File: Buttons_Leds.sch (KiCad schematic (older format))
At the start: 38 parts, among them P11 SwPins, P12 PinLeds, Q2 BC849, Q3 BC849, Q4 BC849, Q5 BC849, SW1 TEC_1, SW2 TEC_1, SW3 TEC_1, SW4 TEC_1

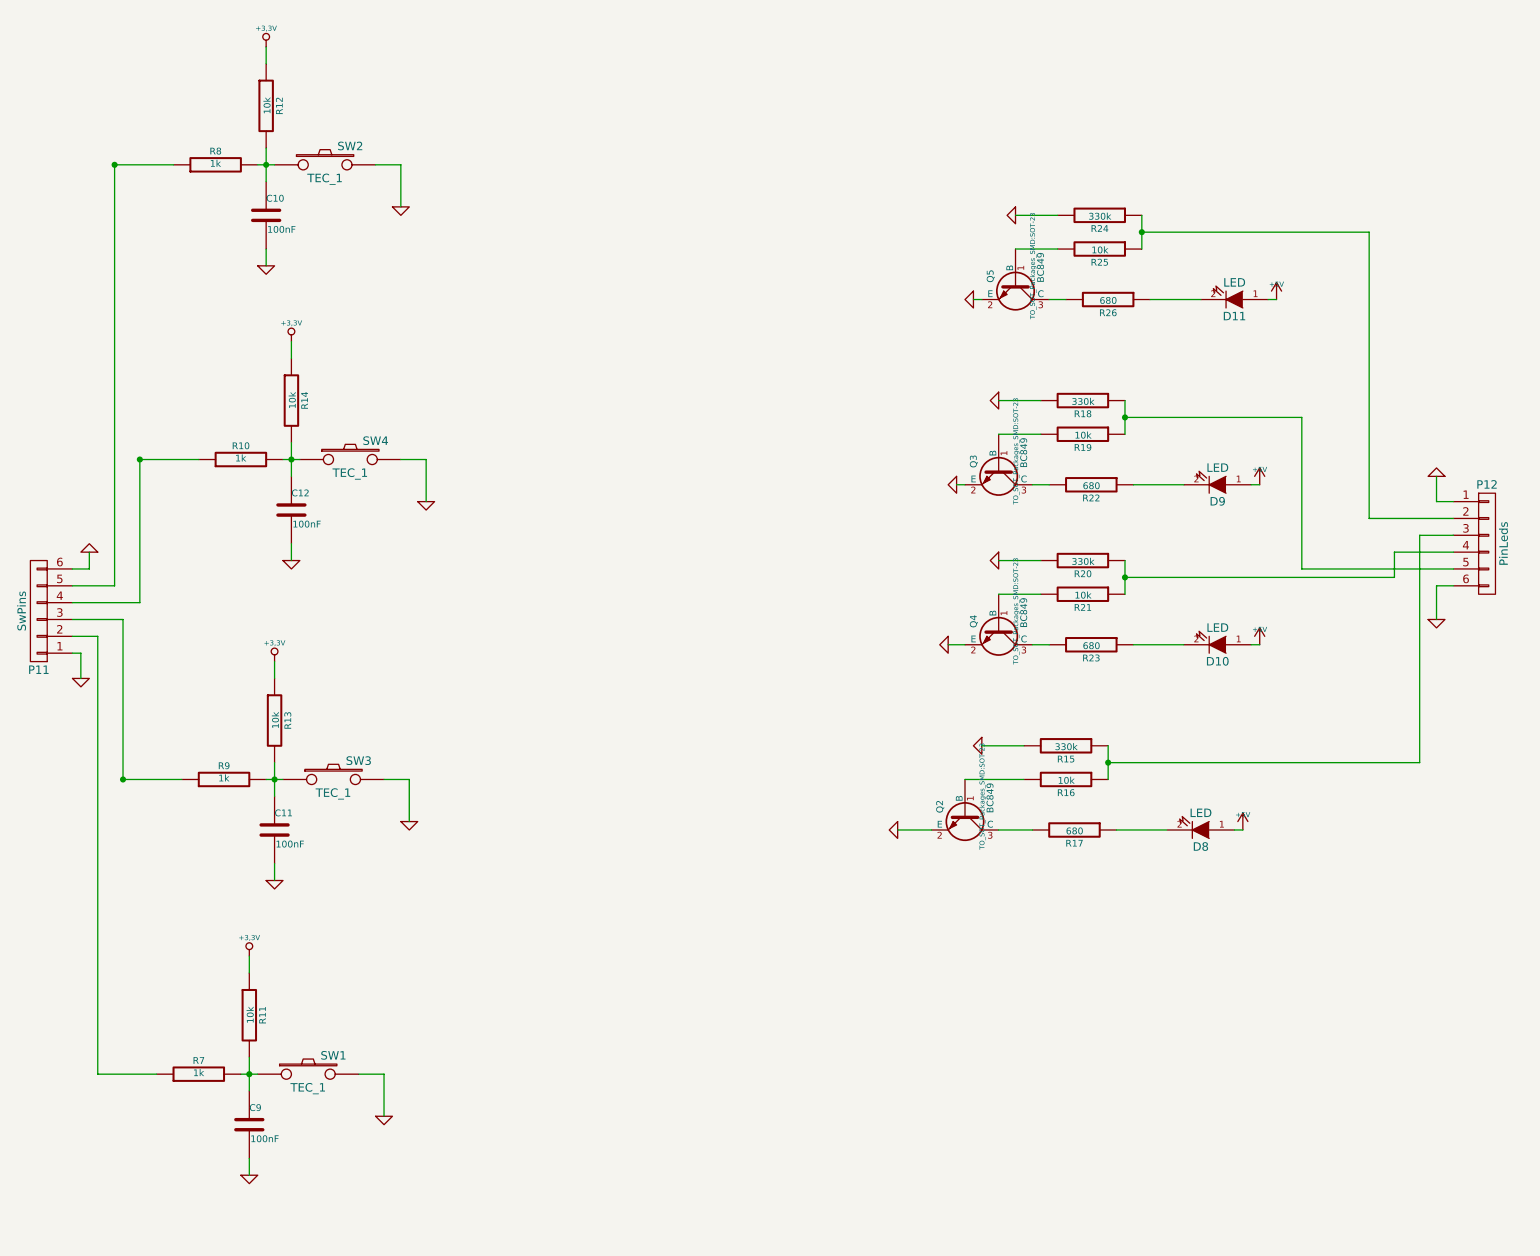
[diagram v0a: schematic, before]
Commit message: Add digikey code and comment schematic.
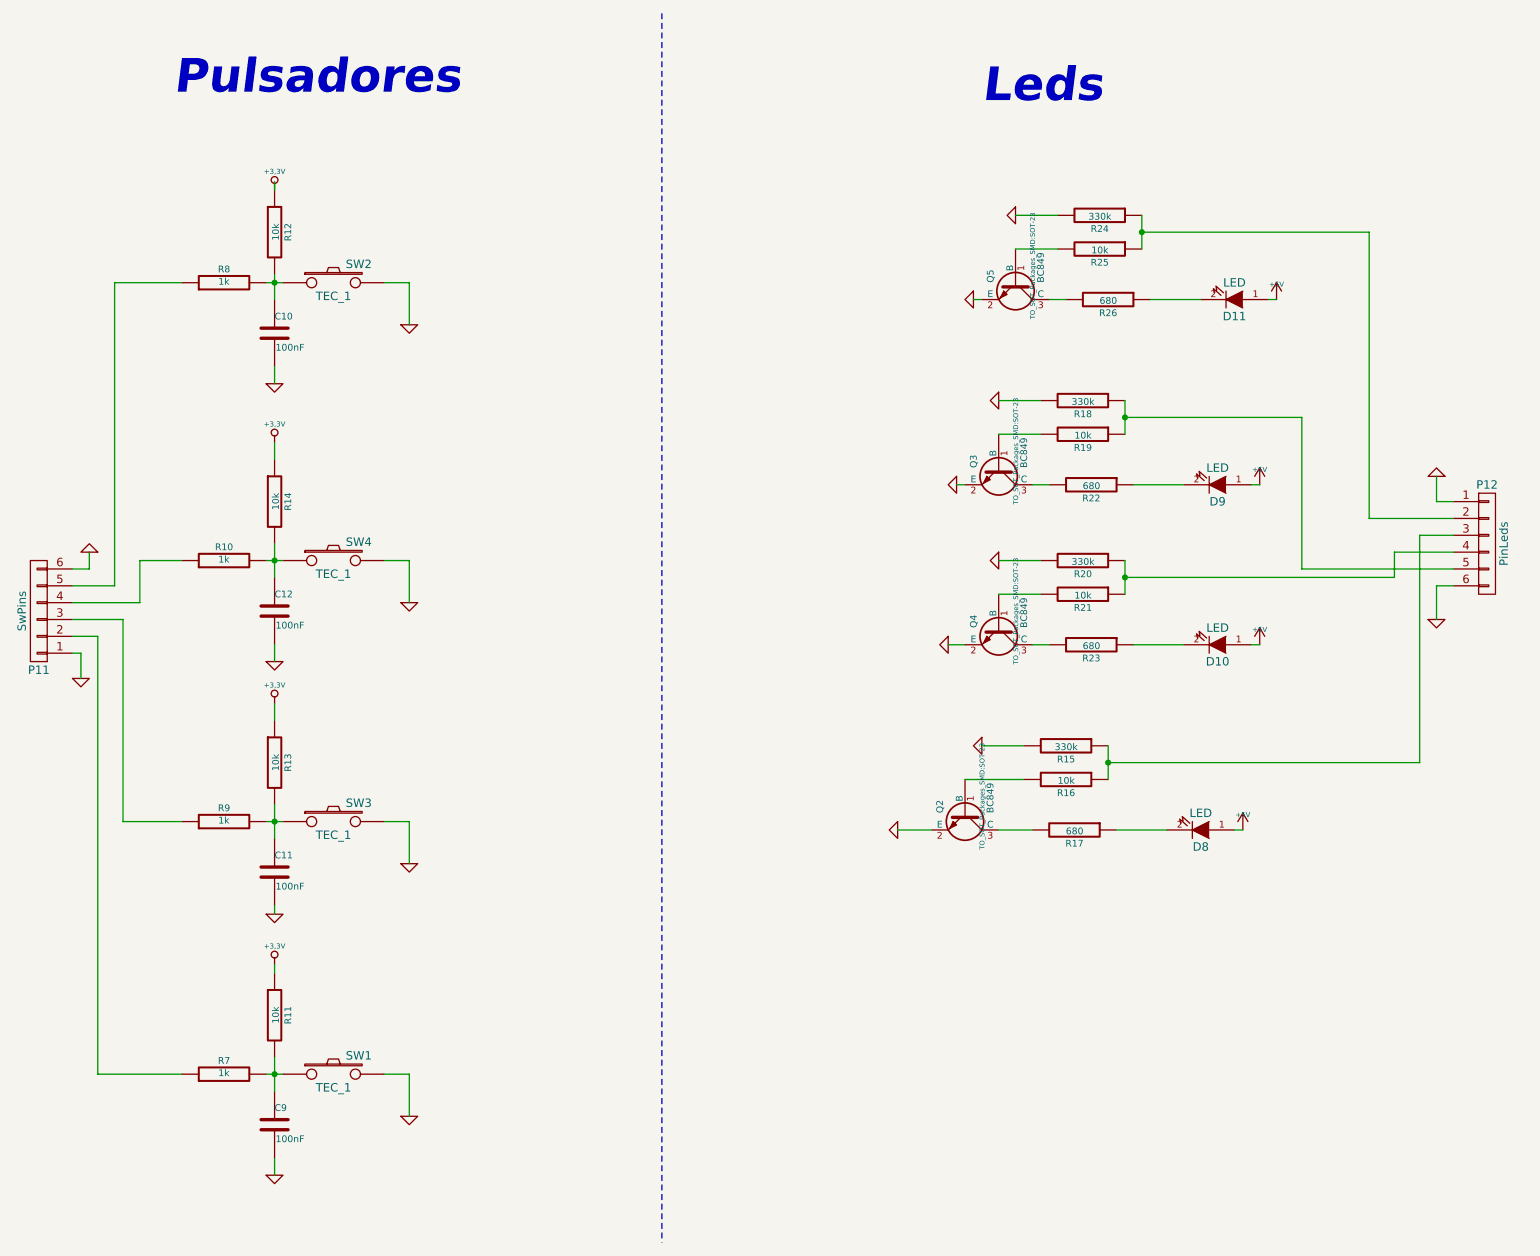
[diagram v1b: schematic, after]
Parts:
- C10, C11, C12, C9: Digikey 399-1167-1-ND -> (none); Digikey# (none) -> 399-1167-1-ND
- D10, D11, D8, D9: Digikey 1080-1410-1-ND -> (none); Digikey# (none) -> 1080-1410-1-ND
- P11, P12: Digikey# (none) -> 1528-1074-ND
- Q2, Q3, Q4, Q5: Digikey# (none) -> BC849BLT1GOSTR-ND
- R10, R7, R8, R9: Digikey 311-1.0KARCT-ND -> (none); Digikey# (none) -> 311-1.0KARCT-ND
- R11, R12, R13, R14, R16, R19, R21, R25: Digikey P10KACT-ND -> (none); Digikey# (none) -> P10KACT-ND
- R15, R18, R20, R24: Digikey RMCF0805JT330KCT-ND -> (none); Digikey# (none) -> RMCF0805JT330KCT-ND
- R17, R22, R23, R26: Digikey RR12P680DCT-ND -> (none); Digikey# (none) -> RR12P680DCT-ND
- SW1, SW2, SW3, SW4: Digikey 450-1804-ND -> (none); Digikey# (none) -> 450-1804-ND
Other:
- note added: "Leds"
- note added: "Pulsadores"
- moved on the sheet: C10, C11, C12, C9, R10, R11, R12, R13, R14, R7, R8, R9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

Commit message: Actualizo las revisiones y documentaciones faltante. Algunas correcciones realizadas, faltan algunas mas que vere de hacerlas.
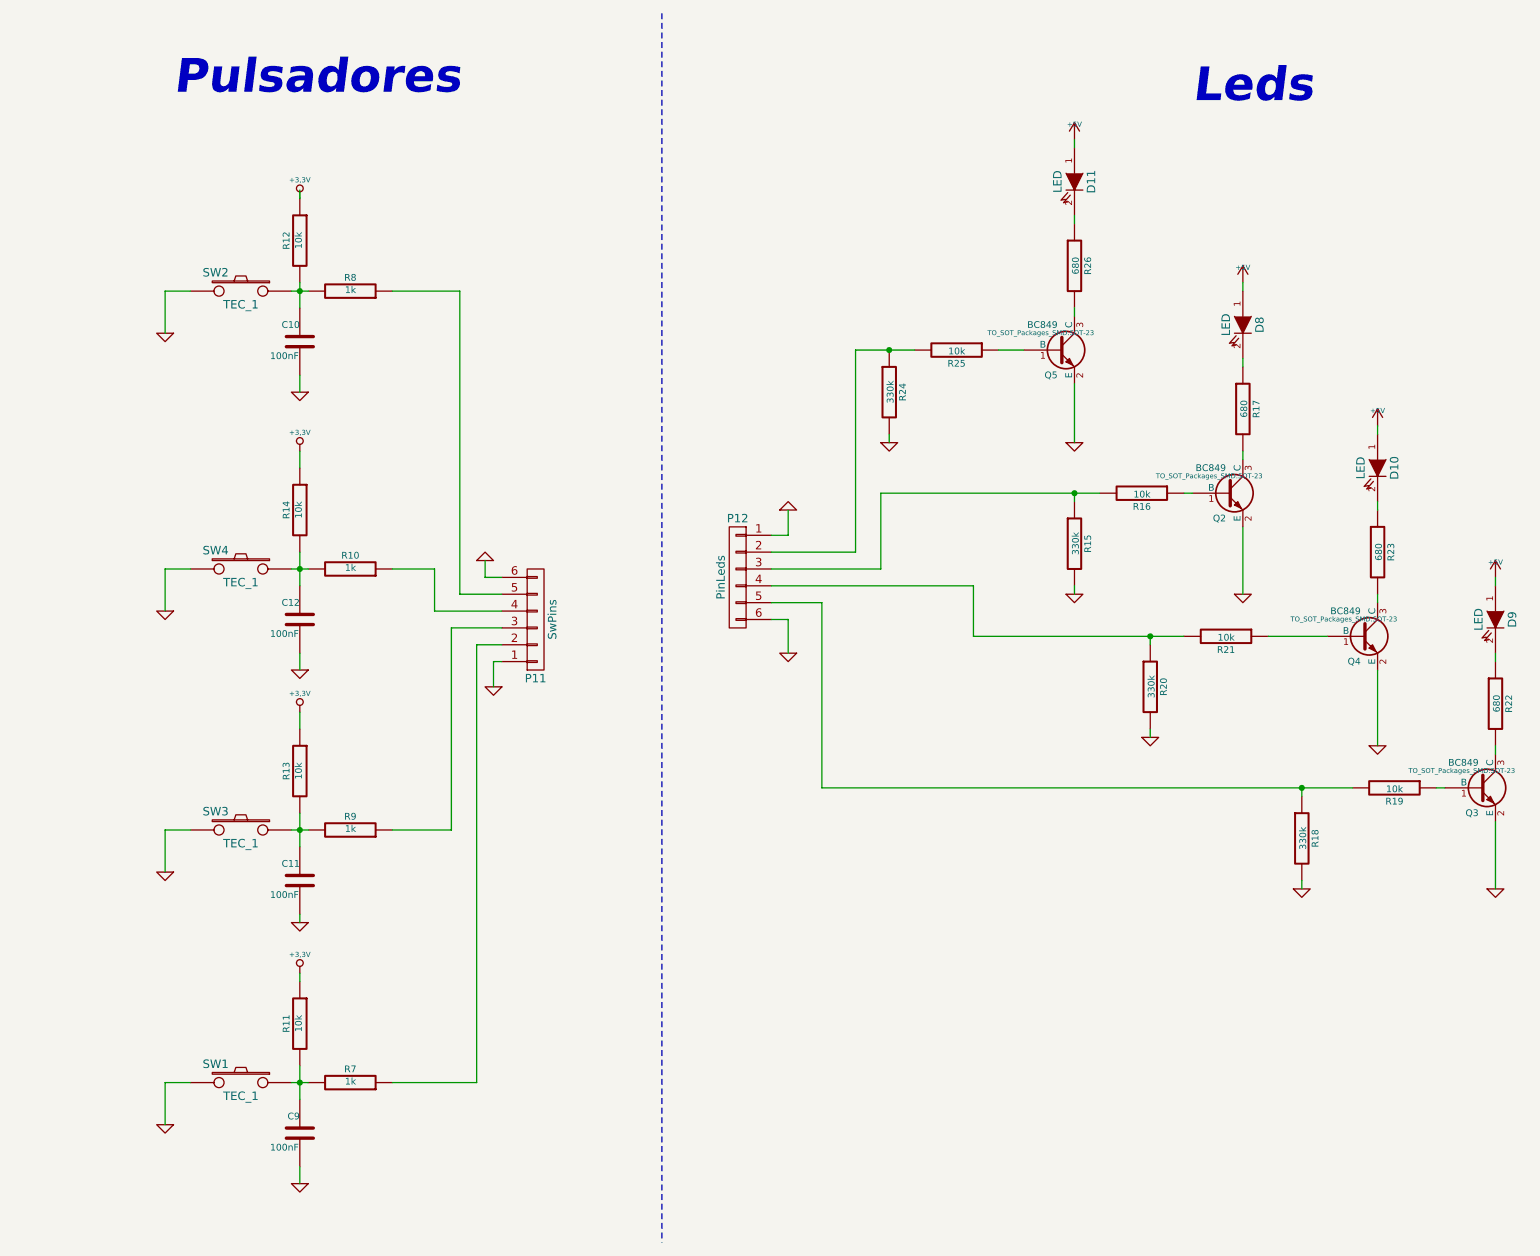
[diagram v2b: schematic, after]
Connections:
- net at P12.4 (P4), R20.1: now also R21.2; no longer R21.1
- net at Q4.1 (B): now also R21.1; no longer R21.2
- net at P12.3 (P3), R15.1: now also R16.2; no longer R16.1
- net at Q2.1 (B): now also R16.1; no longer R16.2
- net at P12.2 (P2), R24.1: now also R25.2; no longer R25.1
- net at Q5.1 (B): now also R25.1; no longer R25.2
- net at P12.5 (P5), R18.1: now also R19.2; no longer R19.1
- net at Q3.1 (B): now also R19.1; no longer R19.2
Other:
- moved on the sheet: C10, C11, C12, C9, D10, D11, D8, D9, P11, P12, Q2, Q3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
